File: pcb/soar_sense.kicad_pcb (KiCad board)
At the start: 2 copper layers, 38 parts, among them J1 Conn_02x03_Top_Bottom, J2 Conn_02x02_Top_Bottom, J3 Conn_02x02_Top_Bottom, J4 Conn_02x02_Top_Bottom, J5 Conn_02x02_Top_Bottom, J6 Conn_02x01, J7 Conn_02x03_Top_Bottom, J8 Conn_02x04_Top_Bottom, U1 SPX3819M5-L-3-3, U2 STM32F103CBTx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

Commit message: today done
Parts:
- removed J2: Conn_02x02_Top_Bottom, OWN_Parts:pcb_edge_2_2
- added C15: 100n, Capacitor_SMD:C_0603_1608Metric, F.Cu at (133.1, 119.4)
- added C16: 100n, Capacitor_SMD:C_0603_1608Metric, F.Cu at (136.4, 110.0)
- added C17: 100n, Capacitor_SMD:C_0603_1608Metric, F.Cu at (129.8, 119.4)
- added C18: 100n, Capacitor_SMD:C_0603_1608Metric, F.Cu at (136.7, 119.4)
- added C19: 100n, Capacitor_SMD:C_0603_1608Metric, F.Cu at (132.8, 122.7)
- added C20: 100n, Capacitor_SMD:C_0603_1608Metric, F.Cu at (143.3, 119.6)
- added D10: D_TVS, Diode_SMD:D_SOD-323, F.Cu at (155.4, 111.3)
- added D11: D_TVS, Diode_SMD:D_SOD-323, F.Cu at (154.7, 108.5)
- added D12: D_TVS, Diode_SMD:D_SOD-323, F.Cu at (156.7, 108.5)
- added D5: D_TVS, Diode_SMD:D_SOD-323, F.Cu at (151.6, 96.3)
- added D6: D_TVS, Diode_SMD:D_SOD-323, F.Cu at (151.6, 98.3)
- added D7: D_TVS, Diode_SMD:D_SOD-323, F.Cu at (154.7, 101.9)
- added D8: D_TVS, Diode_SMD:D_SOD-323, F.Cu at (156.7, 101.9)
- added D9: D_TVS, Diode_SMD:D_SOD-323, F.Cu at (151.9, 111.3)
- added JP1: SolderJumper_2_Open, Jumper:SolderJumper-2_P1.3mm_Open_Pad1.0x1.5mm, F.Cu at (123.7, 106.2)
- added R10: 10k, Resistor_SMD:R_0603_1608Metric, F.Cu at (146.7, 111.3)
- added R11: 10k, Resistor_SMD:R_0603_1608Metric, F.Cu at (141.5, 119.7)
- added R12: 10k, Resistor_SMD:R_0603_1608Metric, F.Cu at (131.6, 119.4)
- added R13: 10k, Resistor_SMD:R_0603_1608Metric, F.Cu at (133.2, 109.2)
- added R14: 10k, Resistor_SMD:R_0603_1608Metric, F.Cu at (128.3, 119.4)
- added R15: 10k, Resistor_SMD:R_0603_1608Metric, F.Cu at (132.8, 124.5)
- added R9: 10k, Resistor_SMD:R_0603_1608Metric, F.Cu at (145.2, 99.1)
- added Y1: 8MHz, Crystal:Crystal_SMD_3225-4Pin_3.2x2.5mm, F.Cu at (136.3, 104.8)
- R2: value 100k -> 120R
- R4: value 100k -> 10k
- moved C7 27.5 mm to (129.3, 107.7)
- moved C9 25.1 mm to (130.8, 107.7)
- moved C4 24.1 mm to (127.8, 107.7), turned to -90 degrees
- moved R4 23.9 mm to (134.9, 119.4)
- moved R2 22.4 mm to (126.0, 106.0)
- moved U1 21.6 mm to (129.3, 103.9), turned to -90 degrees
- moved C14 16.9 mm to (137.7, 99.1), turned to -90 degrees
- moved D3 16.8 mm to (126.7, 99.1), turned to 180 degrees
- moved C1 16.4 mm to (130.0, 100.8), turned to 180 degrees
- moved J6 16.0 mm to (142.2, 95.5), turned to 90 degrees
- moved C2 15.5 mm to (145.3, 97.5), turned to 180 degrees
- moved R1 14.8 mm to (140.5, 96.6), turned to -90 degrees
- moved D1 14.5 mm to (145.3, 95.8), turned to 180 degrees
- moved D2 14.4 mm to (148.4, 95.8), turned to 180 degrees
- moved R8 13.7 mm to (149.1, 98.3)
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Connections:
- J1 pad 1: GND -> BOOT0
- J1 pad 2: GND -> +3V3
- J1 pad 3: BOOT0 -> +3V3
- J1 pad 4: BOOT1 -> GND
- J1 pad 5: +3V3 -> USART1_RX
- J1 pad 6: +3V3 -> USART1_TX
- J8 pad 3: unconnected-(J8-Pad3) -> ADC_INPUT5
- J8 pad 4: ADC_IN4 -> ADC_INPUT4
- J8 pad 5: ADC_IN3 -> ADC_INPUT3
- J8 pad 6: ADC_IN2 -> ADC_INPUT2
- J8 pad 7: ADC_IN1 -> ADC_INPUT1
- J8 pad 8: ADC_IN0 -> ADC_INPUT0
- R2 pad 1: Net-(R2-Pad1) -> CAN_H
- R2 pad 2: BOOT1 -> Net-(JP1-Pad1)
- R4 pad 1: Net-(R4-Pad1) -> ADC_INPUT4
- R4 pad 2: BOOT0 -> ADC_IN4
- U2 pad 15: unconnected-(U2-Pad15) -> ADC_IN5
- U2 pad 20: Net-(R2-Pad1) -> BOOT1
- U2 pad 44: Net-(R4-Pad1) -> BOOT0
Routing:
- net GND: track 0.00 -> 68.9 mm, vias 0 -> 28
- net +3V3: track 0.00 -> 48.3 mm, vias 0 -> 15
- net USART1_RX: track 0.00 -> 31.7 mm, vias 0 -> 2
- net USART1_TX: track 0.00 -> 31.4 mm, vias 0 -> 1
- net BOOT0: track 0.00 -> 27.8 mm, vias 0 -> 2
- net I2C1_SCL: track 0.00 -> 23.0 mm, vias 0 -> 2
- net I2C1_SDA: track 0.00 -> 21.7 mm, vias 0 -> 3
- net SPI2_NSS: track 0.00 -> 20.5 mm, vias 0 -> 2
- net SPI2_SCK: track 0.00 -> 18.7 mm, vias 0 -> 2
- net Net-(C2-Pad1): track 0.00 -> 18.5 mm, vias 0 -> 3
- net SPI2_MISO: track 0.00 -> 17.9 mm, vias 0 -> 2
- net CAN_RX: track 0.00 -> 16.6 mm, vias 0 -> 2
- net SPI2_MOSI: track 0.00 -> 15.9 mm, vias 0 -> 2
- net CAN_L: track 0.00 -> 15.1 mm, vias 0 -> 2
- net CAN_TX: track 0.00 -> 14.5 mm, vias 0 -> 2
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- added copper zone on In2.Cu, net +3V3
- added copper zone on In1.Cu, net GND
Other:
- board outline added: 40.6 x 23.1 mm
- copper layers 2 -> 4

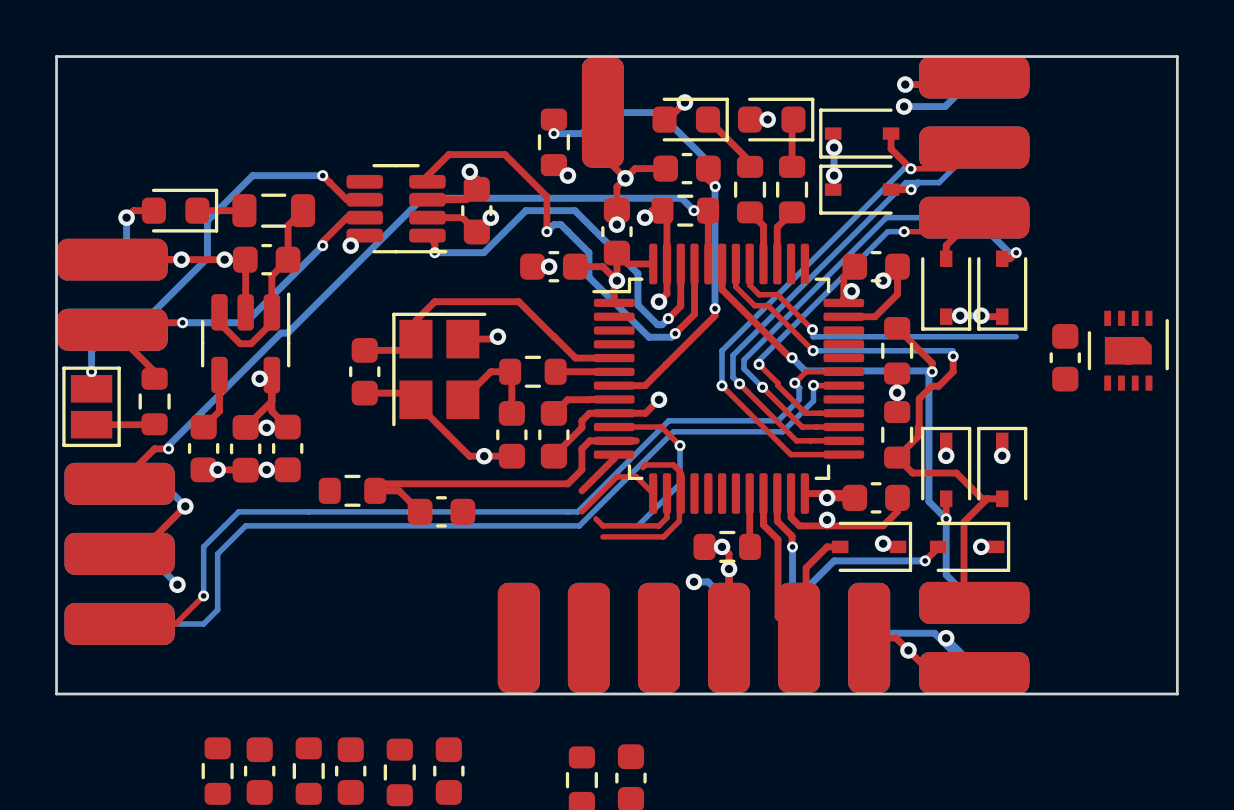
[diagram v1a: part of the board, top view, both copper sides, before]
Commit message: added crystal
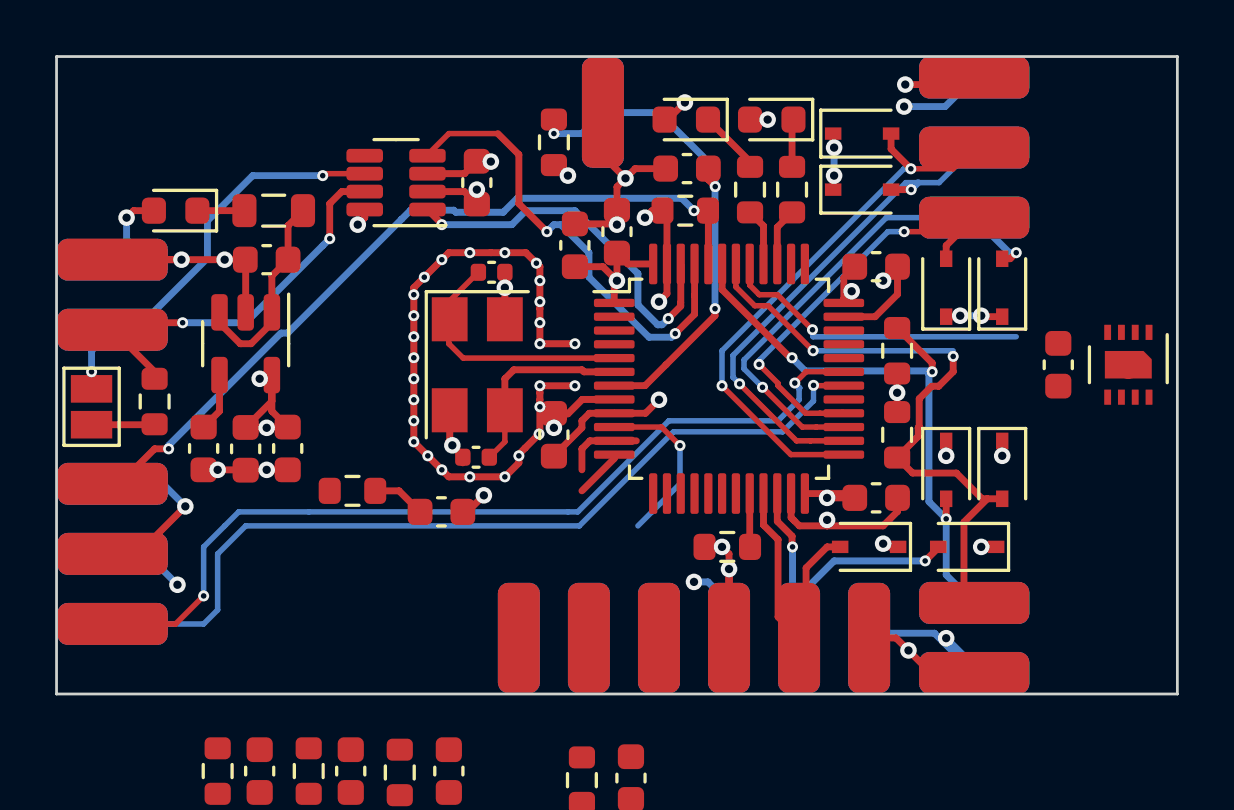
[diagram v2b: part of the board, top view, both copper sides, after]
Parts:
- removed R3: ??Ohm, Resistor_SMD:R_0603_1608Metric
- C3, C5: value ??pF -> 30p; footprint Capacitor_SMD:C_0603_1608Metric -> Capacitor_SMD:C_0402_1005Metric
- Y1: footprint Crystal:Crystal_SMD_3225-4Pin_3.2x2.5mm -> Crystal:Crystal_SMD_5032-4Pin_5.0x3.2mm
- moved C3 5.85 mm to (138.2, 101.3), turned to 0 degrees
- moved C5 1.53 mm to (137.6, 108.0), turned to 180 degrees
- moved Y1 1.38 mm to (137.7, 104.6)
- moved C6 1.09 mm to (141.2, 100.3), turned to 90 degrees
- moved C14 1.02 mm to (137.7, 98.0)
- moved U4 0.95 mm to (134.7, 98.0)
- moved U3 0.51 mm to (161.3, 104.6)
- moved C13 0.36 mm to (158.8, 104.6)
- moved J1 0.25 mm to (124.5, 111.5)
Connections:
- U2 pad 6: Net-(R3-Pad2) -> Net-(C5-Pad1)
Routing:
- net GND: track 68.9 -> 91.2 mm, vias 28 -> 56
- net ADC_IN1: track 12.6 -> 5.16 mm
- net ADC_IN5: track 7.43 -> 0.00 mm
- net ADC_IN4: track 3.68 -> 0.00 mm
- net Net-(C5-Pad1): track 3.67 -> 7.22 mm
- net ADC_IN3: track 3.36 -> 0.00 mm
- net Net-(R3-Pad2): track 2.13 -> 0.00 mm
- net Net-(U2-Pad5): track 11.0 -> 9.25 mm
- net CAN_H: track 13.3 -> 14.4 mm
- net CAN_TX: track 14.5 -> 13.8 mm

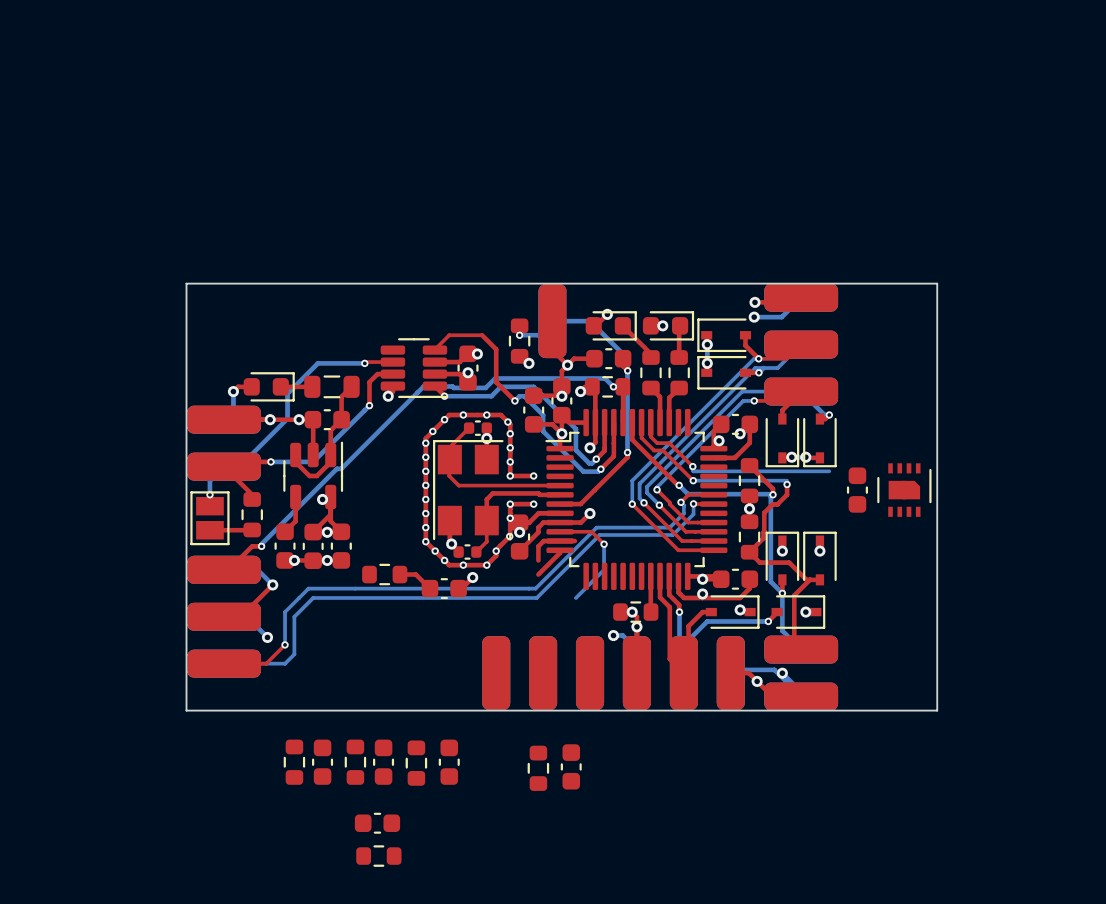
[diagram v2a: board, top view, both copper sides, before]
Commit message: sht connected
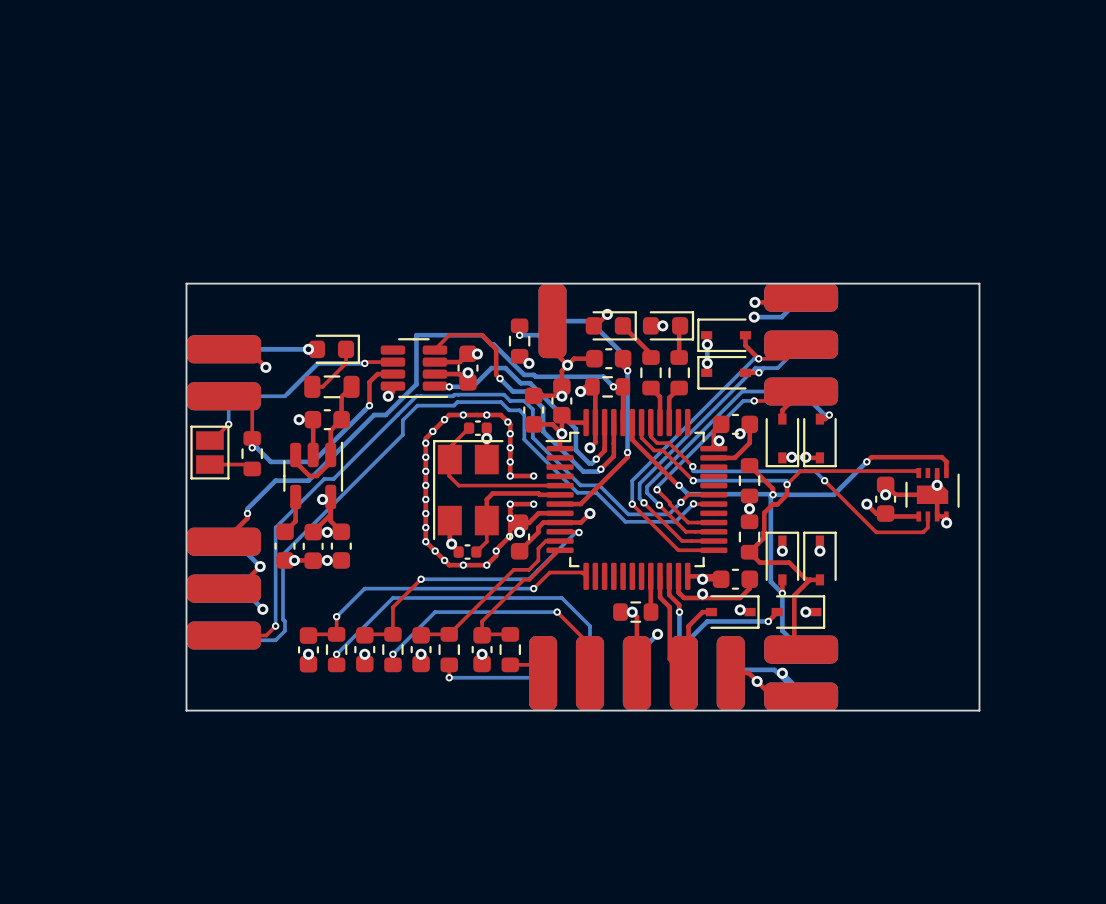
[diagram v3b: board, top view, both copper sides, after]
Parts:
- removed C18, C20: 100n, Capacitor_SMD:C_0603_1608Metric
- removed J8: Conn_02x04_Top_Bottom, OWN_Parts:pcb_edge_2_4
- removed R11, R4: 10k, Resistor_SMD:R_0603_1608Metric
- added J2: Conn_02x03_Top_Bottom, OWN_Parts:pcb_edge_2_3, F.Cu at (144.3, 114.6)
- moved R14 13.2 mm to (140.0, 113.3), turned to 90 degrees
- moved R15 11.2 mm to (133.6, 113.3), turned to 90 degrees
- moved C17 10.6 mm to (138.4, 113.3)
- moved C19 9.42 mm to (132.1, 113.3), turned to -90 degrees
- moved C15 7.32 mm to (129.0, 113.3)
- moved R12 6.18 mm to (130.6, 113.3)
- moved R13 5.36 mm to (136.7, 113.3), turned to 90 degrees
- moved D3 4.07 mm to (130.3, 97.0)
- moved J3 3.81 mm to (124.5, 98.3)
- moved JP1 3.56 mm to (123.7, 102.6)
- moved C16 3.53 mm to (135.1, 113.3), turned to -90 degrees
- moved R2 3.30 mm to (126.0, 102.7)
- moved C13 1.60 mm to (160.3, 105.1)
- moved U3 1.55 mm to (162.8, 104.9)
- moved J1 1.52 mm to (124.5, 110.0)
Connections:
- U2 pad 14: ADC_IN4 -> unconnected-(U2-Pad14)
- U2 pad 15: ADC_IN5 -> unconnected-(U2-Pad15)
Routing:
- net ADC_INPUT3: track 0.00 -> 18.7 mm, vias 0 -> 1
- net ADC_IN3: track 0.00 -> 17.1 mm, vias 0 -> 2
- net ADC_INPUT0: track 0.00 -> 14.4 mm, vias 0 -> 2
- net I2C1_SDA: track 21.7 -> 32.7 mm, vias 3 -> 4
- net ADC_IN0: track 6.21 -> 15.8 mm, vias 1 -> 2
- net I2C1_SCL: track 23.0 -> 30.6 mm
- net USART1_TX: track 31.4 -> 38.9 mm
- net SHT_RST: track 11.3 -> 18.8 mm, vias 1 -> 2
- net USART1_RX: track 31.7 -> 39.1 mm
- net ADC_IN2: track 1.80 -> 8.11 mm
- net ADC_IN1: track 5.16 -> 10.0 mm
- net ADC_INPUT1: track 1.78 -> 5.88 mm, vias 0 -> 1
- net BOOT0: track 27.9 -> 31.2 mm
- net VIN: track 2.83 -> 5.03 mm
- net +3V3: track 48.1 -> 50.1 mm, vias 15 -> 16
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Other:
- board size 40.6 x 23.1 mm -> 42.9 x 23.1 mm

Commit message: added copper heat cooling areas
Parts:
- removed J2: Conn_02x03_Top_Bottom, OWN_Parts:pcb_edge_2_3
- added J8: Conn_01x06, Connector_Molex:Molex_PicoBlade_53048-0610_1x06_P1.25mm_Horizontal, B.Cu at (148.8, 95.2)
- D3: footprint Diode_SMD:D_0603_1608Metric -> Diode_SMD:D_SOD-323
- J6: value Conn_02x01 -> Conn_02x03_Top_Bottom; footprint OWN_Parts:pcb_edge_2_1 -> OWN_Parts:pcb_edge_2_3
- R7, R8: value ?? -> R200
- U4: footprint Package_TO_SOT_SMD:SOT-23-8 -> Package_TO_SOT_SMD:SOT-23-8_Handsoldering
- moved J6 19.2 mm to (144.3, 114.6)
- moved D1 15.0 mm to (130.3, 95.2)
- moved D2 12.7 mm to (135.7, 95.2)
- moved D5 1.08 mm to (152.4, 95.5), turned to -90 degrees
- moved D6 0.92 mm to (152.4, 98.8), turned to 90 degrees
- moved R1 0.70 mm to (140.5, 97.3)
- moved C14 0.33 mm to (138.0, 98.0)
- moved C12 0.13 mm to (152.1, 101.2)
- moved J5 0.05 mm to (155.7, 114.5)
- moved J7 0.05 mm to (155.7, 96.8)
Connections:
- C2 pad 1: Net-(C2-Pad1) -> NRST
- J6 pad 2: Net-(C2-Pad1) -> +3V3
- R1 pad 1: Net-(C2-Pad1) -> NRST
- U2 pad 34: unconnected-(U2-Pad34) -> SWDIO
- U2 pad 37: unconnected-(U2-Pad37) -> SWCLK
- U2 pad 7: Net-(C2-Pad1) -> NRST
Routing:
- net Net-(C2-Pad1): track 18.5 -> 0.00 mm, vias 3 -> 0
- net NRST: track 0.00 -> 18.4 mm, vias 0 -> 2
- net Net-(D1-Pad1): track 2.62 -> 19.9 mm, vias 0 -> 2
- net SWDIO: track 0.00 -> 17.0 mm
- net LED_1: track 2.09 -> 15.6 mm, vias 0 -> 1
- net Net-(D2-Pad1): track 2.01 -> 13.6 mm, vias 0 -> 2
- net SWCLK: track 0.00 -> 8.94 mm
- net Net-(C1-Pad1): track 7.45 -> 10.3 mm
- net +3V3: track 50.1 -> 47.9 mm, vias 16 -> 28
- net GND: track 92.8 -> 91.5 mm, vias 61 -> 74
- net I2C1_SDA: track 32.7 -> 33.8 mm
- net BOOT0: track 31.2 -> 32.2 mm
- net I2C1_SCL: track 30.6 -> 31.6 mm
- net USART1_RX: track 39.1 -> 39.9 mm
- net SPI2_SCK: track 18.7 -> 19.5 mm
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- added copper zone on F.Cu, net +3V3
- added copper zone on F.Cu, net GND
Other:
- board size 42.9 x 23.1 mm -> 42.7 x 23.1 mm
- board text added: "+"
- board text added: "-"
- board text added: "23.2mm"
- board text added: "2_C"
- board text added: "3V3"
- board text added: "42.7mm"
- board text added: "7.4mm"
- board text added: "A0"
- board text added: "A1"
- board text added: "A2"
- board text added: "A3"
- board text added: "B0"
- board text added: "C"
- board text added: "C_H"
- board text added: "C_L"
- board text added: "D"
- board text added: "GND"
- board text added: "I2C2_D"
- board text added: "MISO"
- board text added: "MOSI"
- board text added: "Maximilian Betz"
- board text added: "NRST"
- board text added: "NSS"
- board text added: "SCK"
- board text added: "SENSE"
- board text added: "SOAR"
- board text added: "SWCLK"
- board text added: "SWDIO"
- board text added: "SWO"
- board text added: "U1_RX"
- board text added: "U1_TX"
- board text added: "Vin"
- board text added: "pcbDesign"
- board text added: "the"
